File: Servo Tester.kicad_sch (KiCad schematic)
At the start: 10 parts, among them J1 Conn_01x02_Pin, J2 Conn_01x03_Pin, U1 NE555P

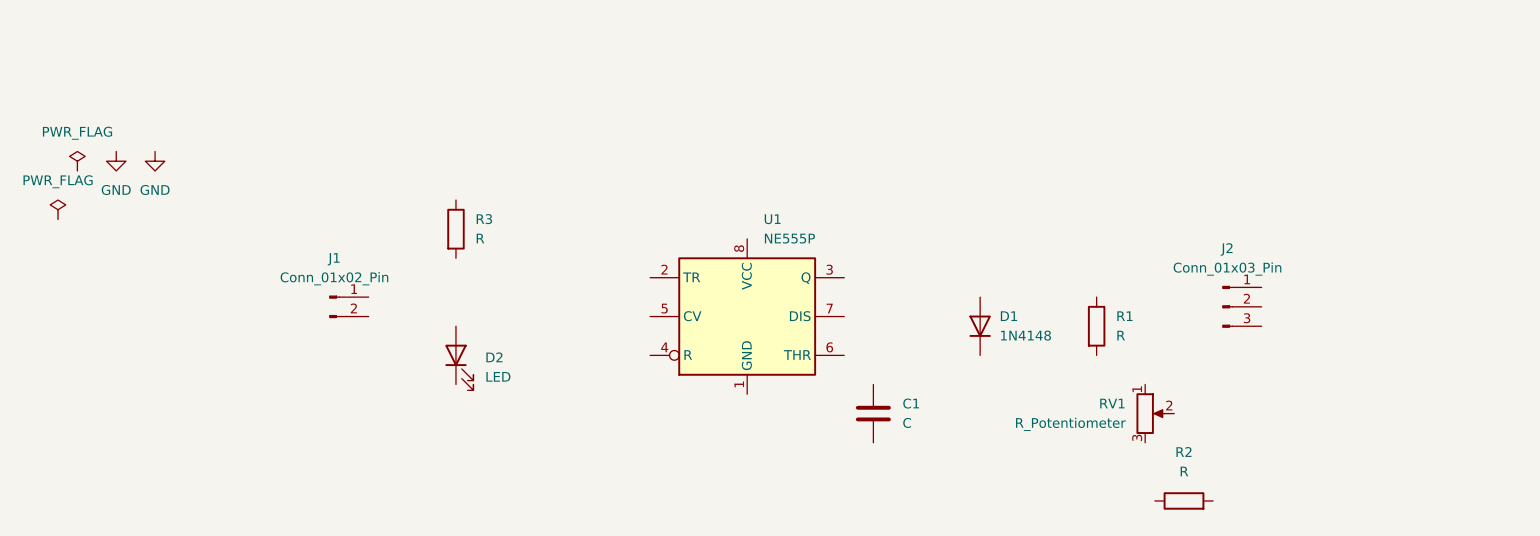
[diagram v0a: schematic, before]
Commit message: Connected All the Components with Wires
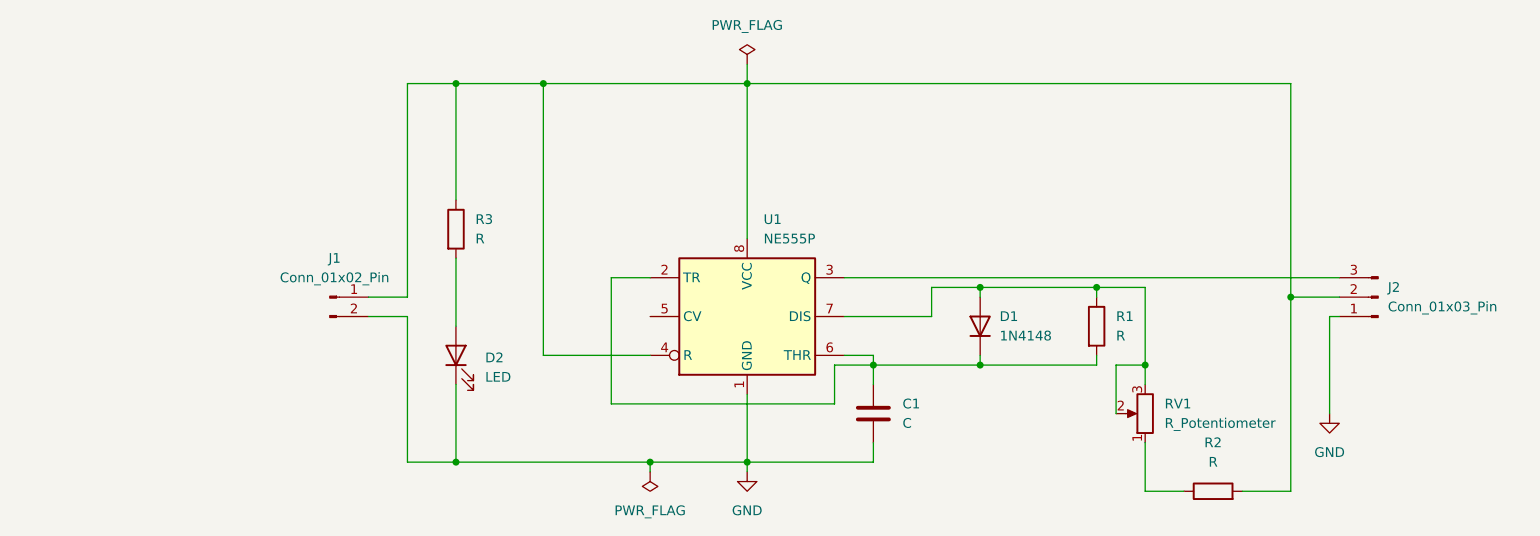
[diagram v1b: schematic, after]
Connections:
- net GND: now also C1.2, D2.1 (K), J1.2 (Pin_2), J2.1 (Pin_1), U1.1 (GND)
- net at D1.1 (K): now also C1.1, R1.2, U1.2 (TR), U1.6 (THR)
- net at D1.2 (A): now also R1.1, RV1.2, RV1.3, U1.7 (DIS)
- net at R2.1: now also RV1.1
- net at R2.2: now also J1.1 (Pin_1), J2.2 (Pin_2), R3.1, U1.4 (R), U1.8 (VCC)
- net at U1.3 (Q): now also J2.3 (Pin_3)
- net at R3.2: now also D2.2 (A)
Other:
- moved on the sheet: J2, R2, RV1

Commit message: Added Values to Components
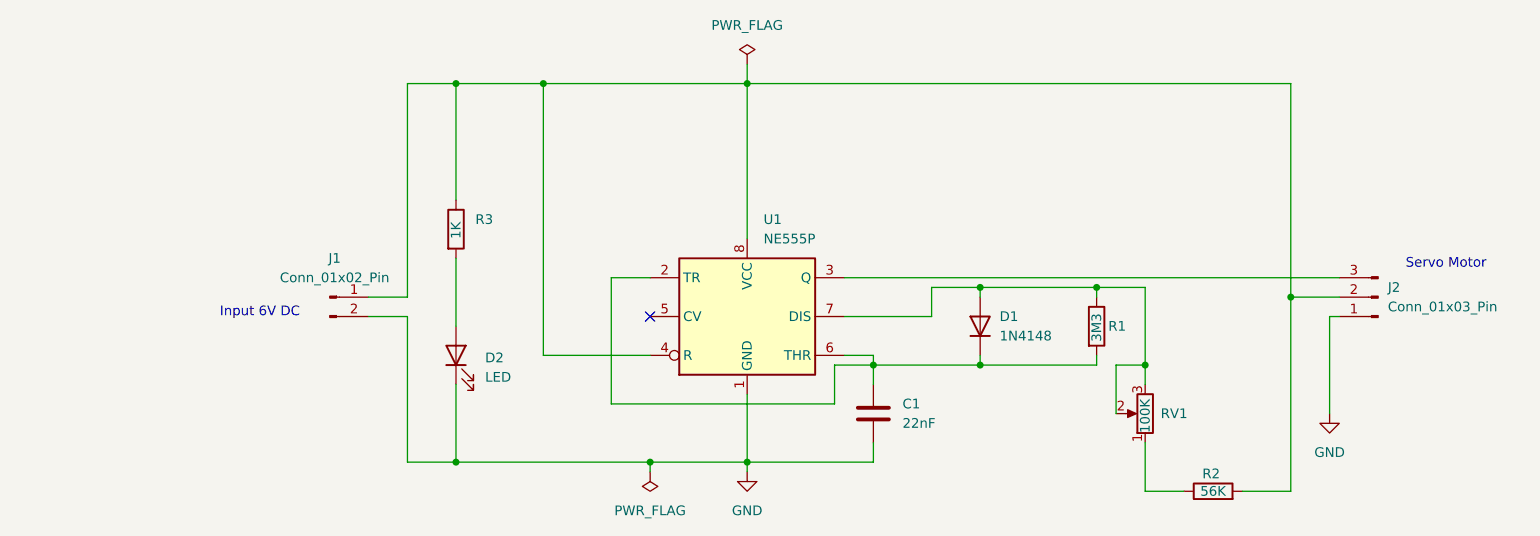
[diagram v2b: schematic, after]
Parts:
- C1: value C -> 22nF
- R1: value R -> 3M3
- R2: value R -> 56K
- R3: value R -> 1K
- RV1: value R_Potentiometer -> 100K
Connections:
- no-connect marks 0 -> 1
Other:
- note added: "Input 6V DC"
- note added: "Servo Motor"
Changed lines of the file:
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@@
 	(generator_version "9.0")
 	(paper "A4")
+	(text "Input 6V DC"
+		(exclude_from_sim no)
+		(at 77.216 96.012 0)
+		(effects
+			(font
+				(size 1.27 1.27)
+			)
+		)
+	)
+	(text "Servo Motor"
+		(exclude_from_sim no)
+		(at 232.41 89.662 0)
+		(effects
+			(font
+				(size 1.27 1.27)
+			)
+		)
+	)
 	(junction
 		(at 171.45 92.71)
@@
 		(diameter 0)
 		(color 0 0 0 0)
+	)
+	(no_connect
+		(at 128.27 96.52)
 	)
 	(wire
@@
 		(on_board yes)
 		(dnp no)
-		(fields_autoplaced yes)
 		(property "Reference" "R2"
-			(at 201.93 113.03 90)
-			(effects
-				(font
-					(size 1.27 1.27)
-				)
-			)
-		)
-		(property "Value" "R"
-			(at 201.93 115.57 90)
+			(at 201.676 117.094 90)
+			(effects
+				(font
+					(size 1.27 1.27)
+				)
+			)
+		)
+		(property "Value" "56K"
+			(at 201.93 119.38 90)
 			(effects
 				(font
@@
 			)
 		)
-		(property "Value" "C"
+		(property "Value" "22nF"
 			(at 161.29 110.4899 0)
 			(effects
@@
 		(on_board yes)
 		(dnp no)
-		(fields_autoplaced yes)
 		(property "Reference" "RV1"
-			(at 195.58 107.9499 0)
+			(at 195.072 109.22 0)
 			(effects
 				(font
@@
 			)
 		)
-		(property "Value" "R_Potentiometer"
-			(at 195.58 110.4899 0)
+		(property "Value" "100K"
+			(at 193.04 111.76 90)
 			(effects
 				(font
@@
 		(on_board yes)
 		(dnp no)
-		(fields_autoplaced yes)
 		(property "Reference" "R1"
-			(at 189.23 96.5199 0)
+			(at 188.214 97.79 0)
 			(effects
 				(font
@@
 			)
 		)
-		(property "Value" "R"
-			(at 189.23 99.0599 0)
+		(property "Value" "3M3"
+			(at 186.69 99.822 90)
 			(effects
 				(font
@@
 		(on_board yes)
 		(dnp no)
-		(fields_autoplaced yes)
 		(property "Reference" "R3"
 			(at 105.41 83.8199 0)
@@
 			)
 		)
-		(property "Value" "R"
-			(at 105.41 86.3599 0)
-			(effects
-				(font
+		(property "Value" "1K"
+			(at 102.87 86.36 90)
+			(effects
+				(font

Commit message: Added Footprints to Schematic Components
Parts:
- C1: footprint (none) -> Capacitor_THT:C_Disc_D4.3mm_W1.9mm_P5.00mm
- D2: footprint (none) -> LED_THT:LED_D3.0mm
- J1: footprint (none) -> Connector_PinHeader_2.54mm:PinHeader_1x02_P2.54mm_Horizontal
- J2: footprint (none) -> Connector_PinHeader_2.54mm:PinHeader_1x03_P2.54mm_Horizontal
- R1, R2, R3: footprint (none) -> Resistor_THT:R_Axial_DIN0204_L3.6mm_D1.6mm_P7.62mm_Horizontal
- RV1: footprint (none) -> Potentiometer_THT:Potentiometer_Alps_RK163_Single_Horizontal
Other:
- note added: "SIG"
- note added: "VCC"
- title: (none) -> KiCAD Servo Tester Project
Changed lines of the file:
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@@
 	(generator_version "9.0")
 	(paper "A4")
+	(title_block
+		(title "KiCAD Servo Tester Project")
+	)
 	(text "Input 6V DC"
 		(exclude_from_sim no)
@@
 		(exclude_from_sim no)
 		(at 232.41 89.662 0)
+		(effects
+			(font
+				(size 1.27 1.27)
+			)
+		)
+	)
+	(text "VCC"
+		(exclude_from_sim no)
+		(at 215.646 93.472 0)
+		(effects
+			(font
+				(size 1.27 1.27)
+			)
+		)
+	)
+	(text "SIG"
+		(exclude_from_sim no)
+		(at 215.9 90.678 0)
 		(effects
 			(font
@@
 			)
 		)
-		(property "Footprint" ""
+		(property "Footprint" "Resistor_THT:R_Axial_DIN0204_L3.6mm_D1.6mm_P7.62mm_Horizontal"
 			(at 201.93 121.158 90)
 			(effects
@@
 			)
 		)
-		(property "Footprint" ""
+		(property "Footprint" "Capacitor_THT:C_Disc_D4.3mm_W1.9mm_P5.00mm"
 			(at 158.4452 113.03 0)
 			(effects
@@
 			)
 		)
-		(property "Footprint" ""
+		(property "Footprint" "Potentiometer_THT:Potentiometer_Alps_RK163_Single_Horizontal"
 			(at 193.04 109.22 0)
 			(effects
@@
 			)
 		)
-		(property "Footprint" ""
+		(property "Footprint" "Connector_PinHeader_2.54mm:PinHeader_1x02_P2.54mm_Horizontal"
 			(at 86.36 93.98 0)
 			(effects
@@
 			)
 		)
-		(property "Footprint" ""
+		(property "Footprint" "Resistor_THT:R_Axial_DIN0204_L3.6mm_D1.6mm_P7.62mm_Horizontal"
 			(at 184.912 97.79 90)
 			(effects
@@
 			)
 		)
-		(property "Footprint" ""
+		(property "Footprint" "Connector_PinHeader_2.54mm:PinHeader_1x03_P2.54mm_Horizontal"
 			(at 223.52 93.98 0)
 			(effects
@@
 			)
 		)
-		(property "Footprint" ""
+		(property "Footprint" "Resistor_THT:R_Axial_DIN0204_L3.6mm_D1.6mm_P7.62mm_Horizontal"
 			(at 101.092 85.09 90)
 			(effects
@@
 			)
 		)
-		(property "Footprint" ""
+		(property "Footprint" "LED_THT:LED_D3.0mm"
 			(at 102.87 101.6 0)
 			(effects
